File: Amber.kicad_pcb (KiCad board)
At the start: 4 copper layers, 120 x 120 mm, 300 parts, among them J1 Barrel_Jack, J11 Conn_02x05_Odd_Even, J12 Bus_M.2_Socket_M, J13 Conn_01x03_Male, J2 RJ45_LINK-PP_LPJG0926HENL_Hor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, J3 USB_C_Receptacle_USB2.0, J4 USB_A_Stacked, J5 AudioJack, J6 HDMI_D_2.0, J7 Micro_SD_Card_Det, J8 SiLabs Mini Debug, J9 Conn_Coaxial, M1 Fan_4pin, Q1 DMP3013SFV-7, Q2 BSZ440N10NS3GATMA1, SW1 SW_USER, SW2 SW_WIPE, T1 PA2467NL, U1 RaspberryPi-CM4Lite, U10 TPD4EUSB30, U11 SiliconLabs-MGM210P, U12 PCM5121PW, U13 TLV74033PDBVR, U14 TPD4EUSB30, U15 TPD4EUSB30, U16 BD9D321EFJ, U17 BD9D321EFJ, U18 74LVC1G07, U19 74LVC1G07, U2 DF40C-100DS-0.4V, U20 LP5569RTWR, U21 PCF85063AT, U22 RT9742GGJ5, U23 TPS23734, U24 TCMT1107, U25 PCF8563TS, U26 74LVC1G07, U27 74LVC1G07, U3 DF40C-100DS-0.4V, U4 CP2102N-Axx-xQFN20, U5 FSUSB42MUX, U6 FSUSB42MUX, U7 FE1.1, U8 TPD4EUSB30, U9 AP2191W, Y1 12MHz/10pF, Y2 32768Hz/12.5pF

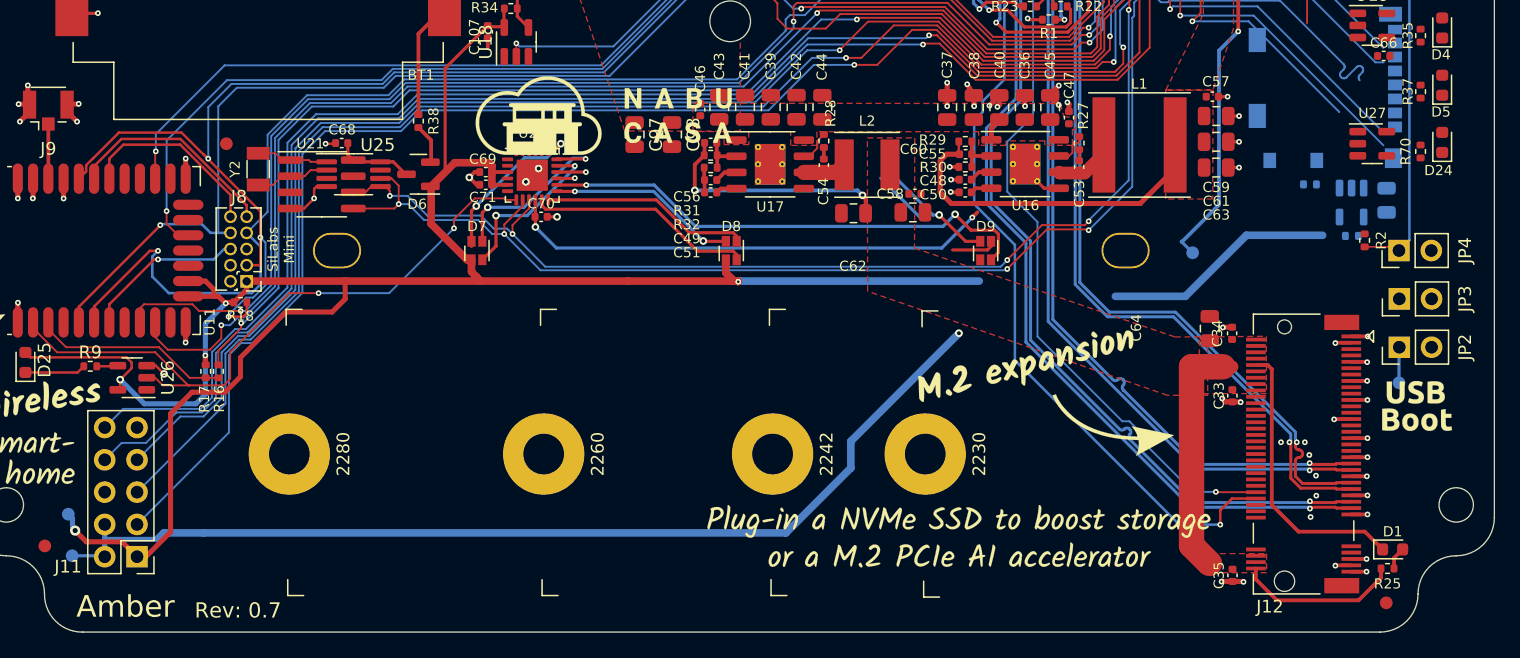
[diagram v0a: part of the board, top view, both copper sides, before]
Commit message: Update silkscreen
- Add new backside silkscreen
- Update USB recovery silkscreen
- Move Nabu Casa logo
- Add ESD warning to silkscreen
- Update PCB name and revision

Signed-off-by: Stefan Agner <stefan@agner.ch>
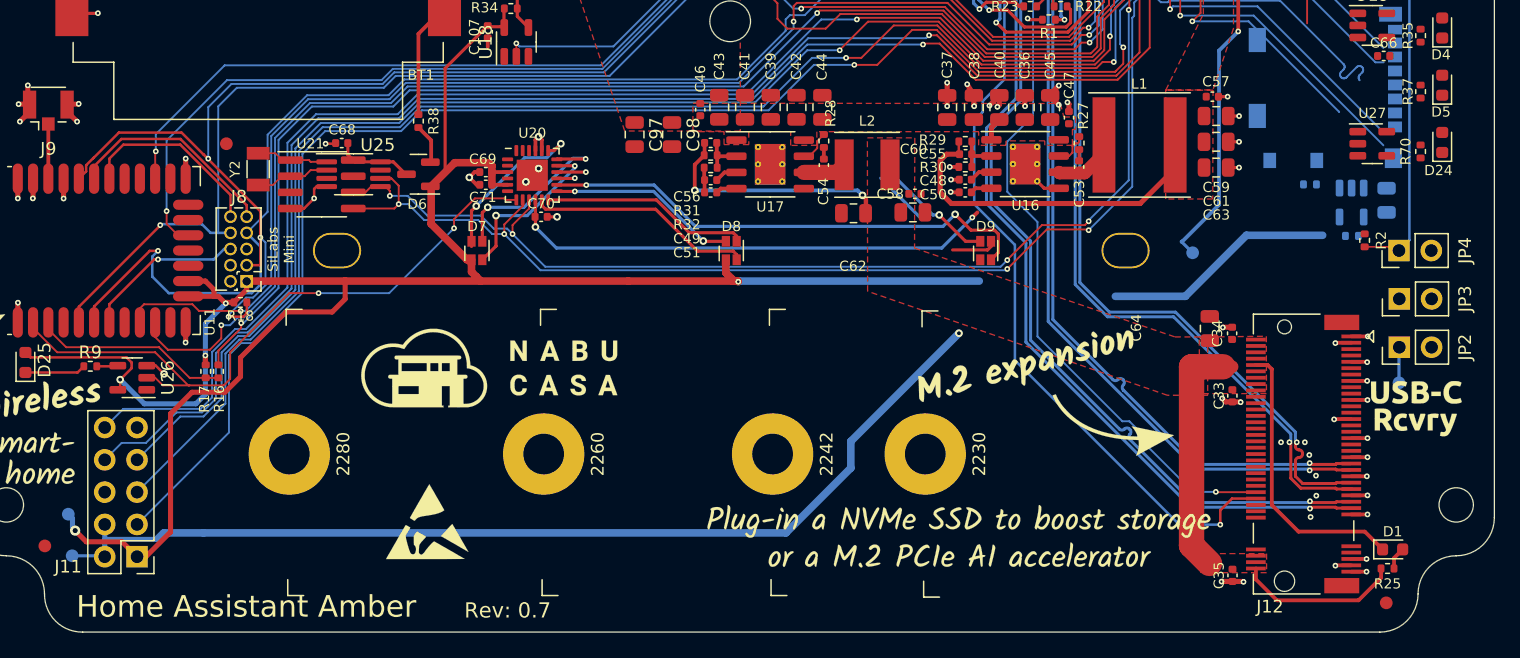
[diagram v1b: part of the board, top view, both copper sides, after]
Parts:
- added REF**: ESD-Logo_6.6x6mm_SilkScreen, Symbol:ESD-Logo_6.6x6mm_SilkScreen, F.Cu at (66.1, 141.3)
- Ref**: footprint Amber:Logo_HomeAssitant_Inverted -> Amber:SilkScreen_AmberBackside; moved to B.Cu
- moved Ref** 21.8 mm to (71.0, 129.2)
- moved Ref** 1.90 mm to (90.0, 90.0), turned to 180 degrees
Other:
- board text added: "Home Assistant Amber"
- board text removed: "Amber"

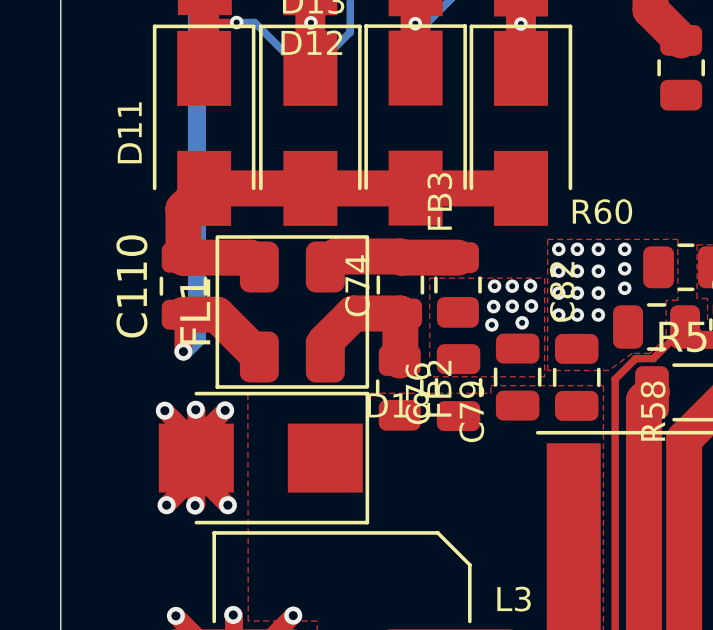
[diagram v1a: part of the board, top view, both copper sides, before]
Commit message: Rename Murata DLW5B
Align with naming of other Common Mode Chokes. Add pin one marking and
reference 3D model.

Signed-off-by: Stefan Agner <stefan@agner.ch>
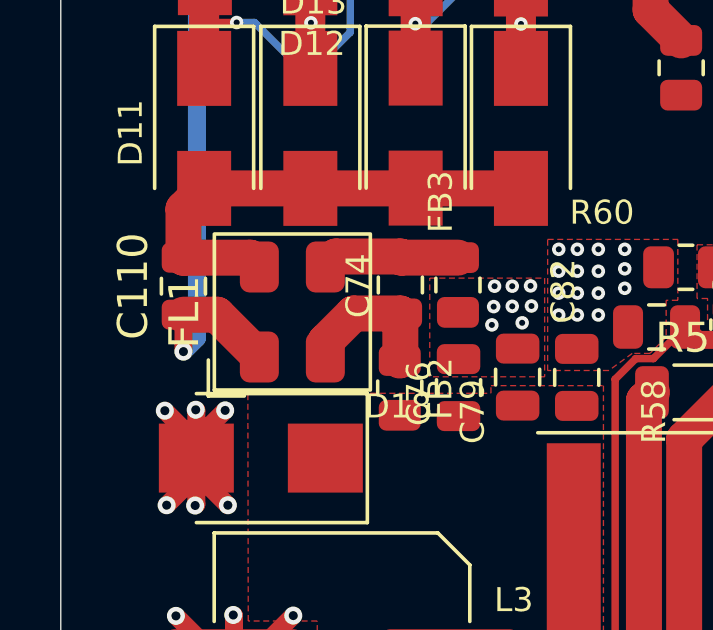
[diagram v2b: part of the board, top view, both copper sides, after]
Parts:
- FL1: footprint Amber:Murata_DLW5B -> Amber:L_CommonModeChoke_Murata_DLW5B
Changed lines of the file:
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@@
     )
   )
-  (footprint "Amber:Murata_DLW5B" (layer "F.Cu")
+  (footprint "Amber:L_CommonModeChoke_Murata_DLW5B" (layer "F.Cu")
     (at 37.72 61.7 90)
+    (descr "Murata DLW5B Series Common Mode Chokes/Fitlers")
+    (tags "surface mount common mode choke")
     (property "Config" "+PoE")
     (property "Manufacturer" "Murata Electronics")
@@
     (property "Sheetfile" "PoE.kicad_sch")
     (property "Sheetname" "PoE")
-    (fp_text reference "FL1" (at 0 -3.2 90 unlocked) (layer "F.SilkS")
+    (fp_text reference "FL1" (at 0 -3.6 90 unlocked) (layer "F.SilkS")
       (effects (font (size 1 1) (thickness 0.15)))
     )
-    (fp_text value "1k@100MHz/500mA" (at 0 4.5 90 unlocked) (layer "F.Fab")
+    (fp_text value "1k@100MHz/500mA" (at 0 5 90 unlocked) (layer "F.Fab")
       (effects (font (size 1 1) (thickness 0.15)))
     )
-    (fp_text user "${REFERENCE}" (at 0 3.3 90 unlocked) (layer "F.Fab")
+    (fp_text user "${REFERENCE}" (at 0 3.6 90 unlocked) (layer "F.Fab")
       (effects (font (size 1 1) (thickness 0.15)))
     )
-    (fp_rect (start -2.5 -2.5) (end 2.5 2.5) (layer "F.SilkS") (width 0.12) (fill none))
-    (fp_rect (start -2.6 -2.6) (end 2.6 2.6) (layer "F.CrtYd") (width 0.05) (fill none))
+    (fp_line (start -2.8 -1.6) (end -2.8 -2.8) (layer "F.SilkS") (width 0.12))
+    (fp_line (start -2.8 -2.8) (end -1.6 -2.8) (layer "F.SilkS") (width 0.12))
+    (fp_rect (start -2.6 -2.6) (end 2.6 2.6) (layer "F.SilkS") (width 0.12) (fill none))
+    (fp_rect (start -2.7 -2.7) (end 2.7 2.7) (layer "F.CrtYd") (width 0.05) (fill none))
+    (fp_line (start -2 -2.5) (end 2.5 -2.5) (layer "F.Fab") (width 0.1))
+    (fp_line (start 2.5 2.5) (end -2.5 2.5) (layer "F.Fab") (width 0.1))
+    (fp_line (start -2.5 -2) (end -2 -2.5) (layer "F.Fab") (width 0.1))
+    (fp_line (start 2.5 -2.5) (end 2.5 2.5) (layer "F.Fab") (width 0.1))
+    (fp_line (start -2.5 2.5) (end -2.5 -2) (layer "F.Fab") (width 0.1))
     (pad "1" smd roundrect (at -1.5 -1.1 90) (size 1.7 1.3) (layers "F.Cu" "F.Paste" "F.Mask") (roundrect_rratio 0.25)
-      (net 113 "Net-(C110-Pad1)") (pinfunction "1") (pintype "passive"))
+      (net 113 "Net-(C110-Pad1)") (pinfunction "1"))
     (pad "2" smd roundrect (at -1.5 1.1 90) (size 1.7 1.3) (layers "F.Cu" "F.Paste" "F.Mask") (roundrect_rratio 0.25)
-      (net 32 "Net-(C74-Pad1)") (pinfunction "2") (pintype "passive"))
+      (net 32 "Net-(C74-Pad1)") (pinfunction "2"))
     (pad "3" smd roundrect (at 1.5 1.1 90) (size 1.7 1.3) (layers "F.Cu" "F.Paste" "F.Mask") (roundrect_rratio 0.25)
-      (net 42 "Net-(C74-Pad2)") (pinfunction "3") (pintype "passive"))
+      (net 42 "Net-(C74-Pad2)") (pinfunction "3"))
     (pad "4" smd roundrect (at 1.5 -1.1 90) (size 1.7 1.3) (layers "F.Cu" "F.Paste" "F.Mask") (roundrect_rratio 0.25)
-      (net 114 "Net-(C110-Pad2)") (pinfunction "4") (pintype "passive"))
+      (net 114 "Net-(C110-Pad2)") (pinfunction "4"))
+    (model "${KIPRJMOD}/Amber.3dshapes/L_CommonModeChoke_Murata_DLW5B.wrl"
+      (offset (xyz 0 0 0))
+      (scale (xyz 1 1 1))
+      (rotate (xyz 0 0 0))
+    )
   )
   (footprint "Package_QFP:TQFP-48_7x7mm_P0.5mm" (layer "F.Cu")

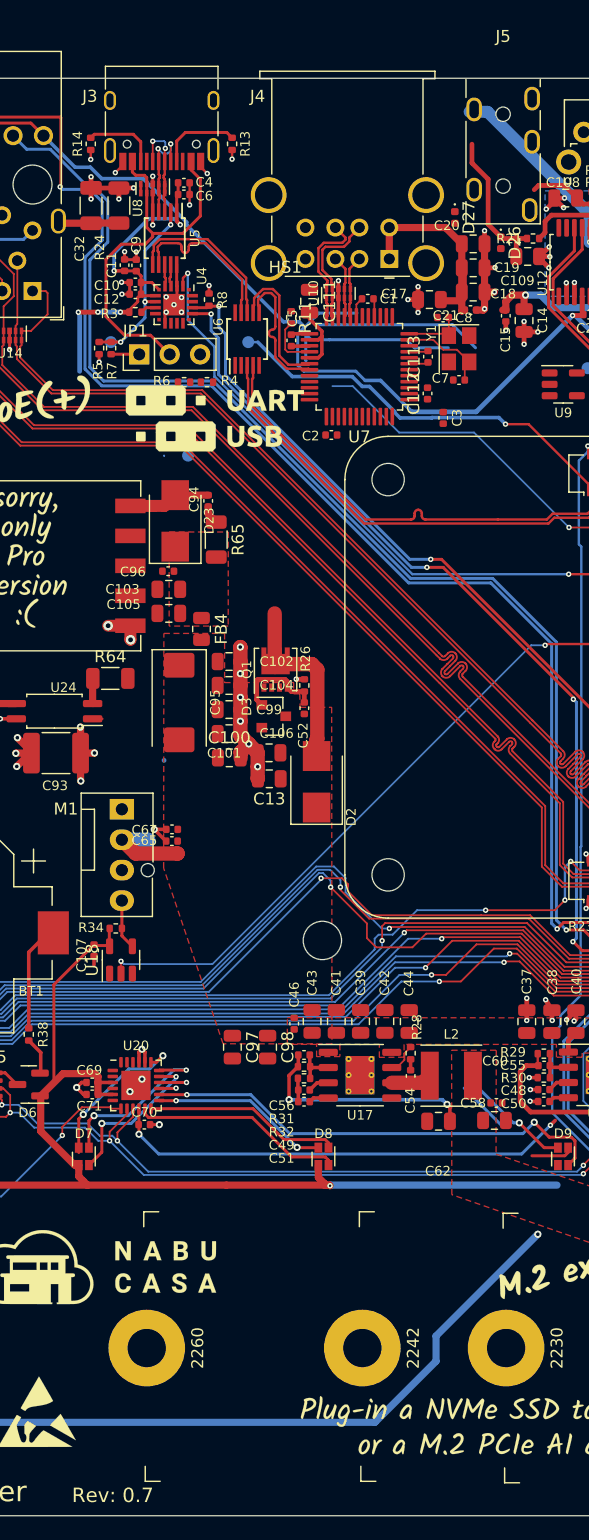
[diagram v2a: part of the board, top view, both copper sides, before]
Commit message: Small Silkscreen/Model improvements
- Move J5 silkscreen to be on the PCB
- Use almost matching Model for CP2102N in QFN20 pacakge
- Bump revision to 1.0

Signed-off-by: Stefan Agner <stefan@agner.ch>
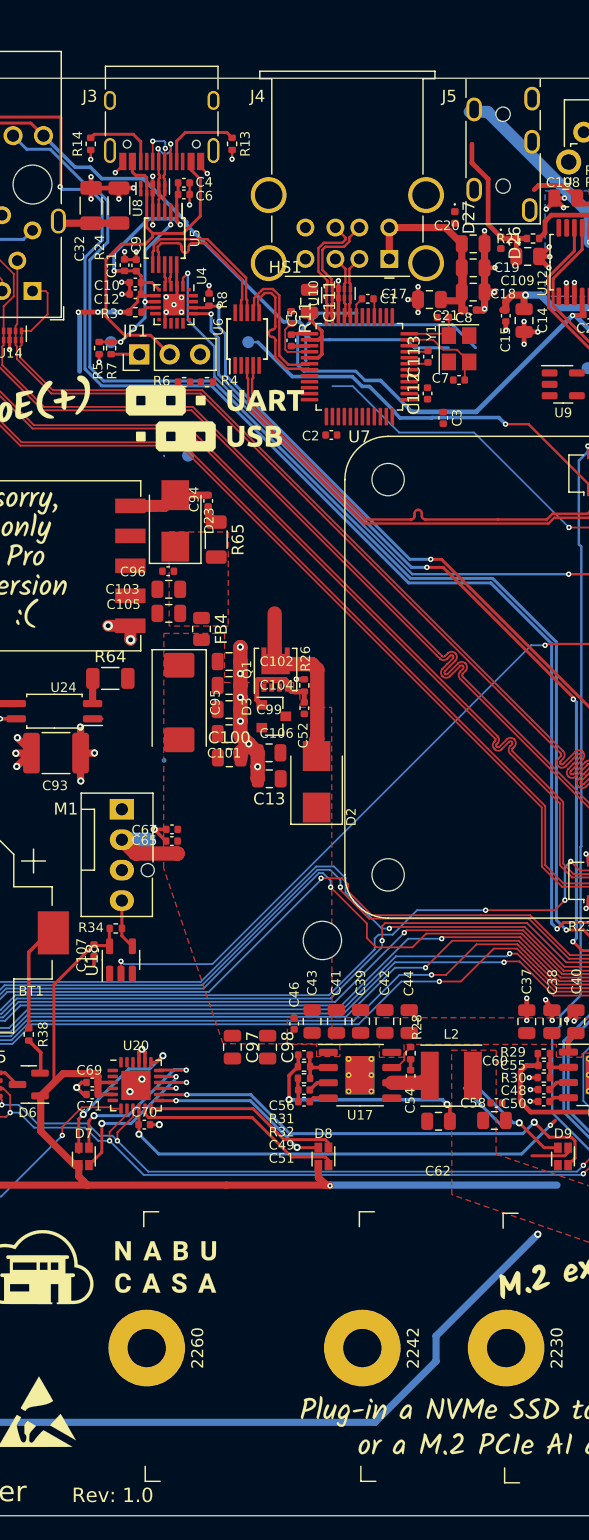
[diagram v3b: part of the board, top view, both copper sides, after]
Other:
- board text added: "Rev: 1.0"
- board text removed: "Rev: 0.7"
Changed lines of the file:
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@@
     (pad "21" smd rect locked (at 0 0 270) (size 1.8 1.8) (layers "F.Cu" "F.Mask")
       (net 2 "GND") (pinfunction "GND") (pintype "passive"))
-    (model "${KICAD6_3DMODEL_DIR}/Package_DFN_QFN.3dshapes/SiliconLabs_QFN-20-1EP_3x3mm_P0.5mm_EP1.8x1.8mm.wrl"
+    (model "${KICAD6_3DMODEL_DIR}/Package_DFN_QFN.3dshapes/QFN-16-1EP_3x3mm_P0.5mm_EP1.8x1.8mm.wrl"
       (offset (xyz 0 0 0))
       (scale (xyz 1 1 1))
@@
     (property "Sheetname" "Audio")
     (attr through_hole)
-    (fp_text reference "J5" (at 0 -3.5) (layer "F.SilkS")
+    (fp_text reference "J5" (at -4.5 1.5) (layer "F.SilkS")
       (effects (font (size 1 1) (thickness 0.15)))
     )
@@
     (effects (font (size 0.8 0.8) (thickness 0.15)))
   )
-  (gr_text "Rev: 0.7" (at 69 148.3) (layer "F.SilkS")
+  (gr_text "Rev: 1.0" (at 69 148.3) (layer "F.SilkS")
     (effects (font (size 1.2 1.2) (thickness 0.15)) (justify left))
   )
